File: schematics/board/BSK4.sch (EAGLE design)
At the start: 33 parts

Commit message: Сделаны платы CROSSnew, SPIDERnew, BSK2
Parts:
- removed DS18B20Z: DS18B20Z, CanCubeSat:DS18B20Z
- removed FS8205A#1, FS8205A#2: FS8205A+, CanCubeSat:FS8205A+
- removed L293DD: L293DD, CanCubeSat:L293DD
- removed LAP4: LAP4-BOTTOM, led:LAP4-BOTTOM
- removed LED1, LED2, LED3, LED4, LED5: (no value), led:LEDCHIPLED_0603
- removed R1, R3, R4, R5, R81: 2k, resistor:R-US_R0603
- removed R10, R11, R2, R7: 100R, resistor:R-US_R0603
- removed R19: 1M, resistor:R-US_R0603
- removed R20: 510k, resistor:R-US_R0603
- removed U$6, U$7: EM_HEAT, CanCubeSat:EM_HEAT
- added DS18B20Z1: DS18B20Z, CanCubeSat:DS18B20Z
- added LAP1: LAP4-BOTTOM, led:LAP4-BOTTOM
- added LED6, LED7: (no value), led:LEDCHIPLED_0603
- added R12, R8: 2M, resistor:R-US_R0603
- added R13, R14: 2k, resistor:R-US_R0603
- added R15, R17, R6, R9: 1M, resistor:R-US_R0603
- added R16: 1k5, resistor:R-US_R0603
- added R94, R95: 2k26, resistor:R-US_R0603
- added U$13, U$8: SI2302CDS, CanCubeSat:SI2302CDS
- added U$14: EM_HEAT, CanCubeSat:EM_HEAT
- added U$26: FS8205A+, CanCubeSat:FS8205A+
- added U$5: MOCD217M, CanCubeSat:MOCD217M
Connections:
- removed net N$1: L293DD.OUT1, LED1.C, LED2.A, U$6.5V
- removed net N$10: LED3.C, R3.1
- removed net N$2: L293DD.OUT2, R1.1, R81.1, U$6.GND
- removed net N$27: LAP4.A, LED4.A, R4.2
- removed net N$28: LED5.A, R5.2
- removed net N$3: L293DD.OUT4, LED3.A, U$7.5V
- removed net N$4: FS8205A#2.G1, R2.2
- removed net N$5: LED2.C, R81.2
- removed net N$6: FS8205A#2.G2, R7.2
- removed net N$7: LED1.A, R1.2
- removed net N$8: FS8205A#1.G1, R10.2
- removed net N$9: FS8205A#1.G2, R11.2
- new net 1: R14.2, U$14.GND, U$8.D
- new net 2: R16.2, U$13.D
- new net B4-KHEAT: R15.1, U$8.G
- new net B4-KVCC: R94.2, R95.2, U$5.AN1, U$5.AN2
- new net B4-ROZE: R17.1, U$13.G
- new net N$29: R6.1, R8.2, U$26.G2
- new net N$30: R12.1, R9.1, U$26.G1
- new net N$31: LAP1.A, R13.2
- new net N$32: LED6.C, R14.1
- new net N$33: LED7.C, R16.1
- new net N$34: DS18B20Z1.HEAT, U$26.HEAT
- new net OC1: R9.2, U$5.COL2
- new net OD1: R6.2, U$5.COL1
- net 1W: now also DS18B20Z1.DQ; no longer DS18B20Z.DQ
- net 5V: now also DS18B20Z1.VDD, LED6.A, R13.1, U$14.5V; no longer DS18B20Z.VDD, L293DD.EN1, L293DD.EN2, L293DD.VS, L293DD.VSS, R4.1, R5.1
- net B4_KEM+: no longer L293DD.IN1
- net B4_KEM-: no longer L293DD.IN2
- net B4_KHEAT: no longer L293DD.IN4
- net B4_KVCC: no longer R10.1, R11.1, R19.1, R20.1
- net BUS+: now also LED7.A, R12.2, R8.1; no longer R19.2
- net BUS-: now also LAP1.C, U$26.S2, U$5.EM1; no longer FS8205A#1.S1, LAP4.C, LED4.C, R20.2
- net GND: now also DS18B20Z1.GND, R15.2, R17.2, R94.1, R95.1, U$13.S, U$26.S1, U$5.CAT1, U$5.CAT2, U$5.EM2, U$8.S; no longer DS18B20Z.GND, DS18B20Z.HEAT, FS8205A#1.HEAT, FS8205A#1.S2, FS8205A#2.HEAT, FS8205A#2.S2, L293DD.GND, L293DD.HEAT, R3.2, U$7.GND
- net PL-: no longer FS8205A#2.S1, LED5.C
- net PL_KVCC: no longer R2.1, R7.1
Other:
- note removed: "EM"

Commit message: Плата АB+DC-DC
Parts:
- removed BSK1: (no value), pinheadCS:PINHD-1X14
- removed LAP1: LAP4-BOTTOM, led:LAP4-BOTTOM
- removed PAYLOAD: (no value), pinheadCS:PINHD-1X8
- removed R15, R17: 1M, resistor:R-US_R0603
- removed R16: 1k5, resistor:R-US_R0603
- removed U$18, U$19, U$20, U$21: KCONNECT, CanCubeSat:KCONNECT
- added BKU: (no value), pinheadCS:PINHD-1X11
- added C41: 0,1µ, rcl:C-USC0603
- added CMD: KCONNECTQUAD, CanCubeSat:KCONNECTQUAD
- added R1, R2: 2k26, resistor:R-US_R0603
- added R4, R7: 2k, resistor:R-US_R0603
- added R5: 100R, resistor:R-US_R0603
- added R75: R01, rcl:R-US_R2512
- added R76, R77: 10R, resistor:R-US_R0603
- added U$10, U$11, U$12, U$9: KCONNECT, CanCubeSat:KCONNECT
- added U$15, U$16, U$6, U$7: GRAFITGRAFIT3_1, CanCubeSat:GRAFITGRAFIT3_1
- added U$57: INA219AID, CanCubeSat:INA219AID
- added YELLOW: LAP4-BOTTOM, led:LAP4-BOTTOM
- R12: value 2M -> 100k
- R13: value 2k -> 1k5
- R14: value 2k -> 1M
- R6: value 1M -> 100k
- R8: value 2M -> 1M
- R9: value 1M -> 100R
- R94, R95: value 2k26 -> 200k
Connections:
- net BUS+1 renamed SP+1
- net BUS-1 renamed SP-1
- removed net B4_KEM+: BSK1.11
- removed net B4_KEM-: BSK1.10
- removed net B4_KHEAT: BSK1.12
- removed net B4_KVCC: BSK1.13
- removed net BUS+2: U$18.P$1
- removed net BUS+3: U$20.P$1
- removed net BUS-: LAP1.C, U$2.P$1, U$26.S2, U$5.EM1
- removed net BUS-2: U$19.P$1
- removed net BUS-3: U$21.P$1
- removed net I2CINT: BSK1.5, PAYLOAD.6
- removed net N$32: LED6.C, R14.1
- removed net N$33: LED7.C, R16.1
- removed net N$34: DS18B20Z1.HEAT, U$26.HEAT
- removed net PL-: PAYLOAD.1
- removed net PL_KVCC: BSK1.8
- removed net SCLTM: BSK1.7, PAYLOAD.8
- removed net SDATM: BSK1.6, PAYLOAD.7
- removed net TIME: BSK1.4, PAYLOAD.5
- removed net VDD: BSK1.1, PAYLOAD.2
- new net 3V3: BKU.8, U$57.A1, U$57.VS
- new net B4-CMD: BKU.4, CMD.P$1
- new net N$150: C41.1, R76.2, U$57.IN+
- new net N$151: C41.2, R77.2, U$57.IN-
- new net N$17: R1.1, R94.2, U$5.AN1
- new net N$18: R2.1, R95.2, U$5.AN2
- new net N$26: R5.1, R6.2, U$26.G2
- new net N$28: R4.2, YELLOW.A
- new net SCL-INA: BKU.10, U$57.SCL
- new net SDA-INA: BKU.11, U$57.SDA
- new net SP+: R75.1, R77.1, U$3.P$1
- new net SP+2: U$9.P$1
- new net SP+3: U$11.P$1
- new net SP-: U$2.P$1, U$26.S2, U$5.EM1, YELLOW.C
- new net SP-2: U$10.P$1
- new net SP-3: U$12.P$1
- net 1: now also R7.2; no longer R14.2
- net 1W: now also BKU.5; no longer BSK1.14
- net 2: now also R13.2, U$15.P$1, U$16.P$1, U$6.P$1, U$7.P$1; no longer R16.2
- net 5V: now also BKU.7, R4.1; no longer BSK1.2, PAYLOAD.3, R13.1
- net B4-KHEAT: now also BKU.1, R8.1; no longer R15.1
- net B4-KVCC: now also BKU.2, R1.2, R2.2; no longer R94.2, R95.2, U$5.AN1, U$5.AN2
- net B4-ROZE: now also BKU.3, R14.1; no longer R17.1
- net BUS+: now also BKU.6, R6.1, R75.2, R76.1, U$15.P$2, U$16.P$2, U$6.P$2, U$7.P$2; no longer BSK1.3, PAYLOAD.4, R8.1, U$3.P$1
- net GND: now also BKU.9, DS18B20Z1.HEAT, R14.2, R8.2, U$26.HEAT, U$57.A0, U$57.GND; no longer BSK1.9, R15.2, R17.2
- net N$29: now also LED7.C, R13.1; no longer R6.1, R8.2, U$26.G2
- net N$31: now also LED6.C, R7.1; no longer LAP1.A, R13.2
- net OD1: now also R5.2; no longer R6.2
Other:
- moved on the sheet: LED6, LED7, R12, R13, R14, R6, R8, R9, R94, R95, U$1, U$2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

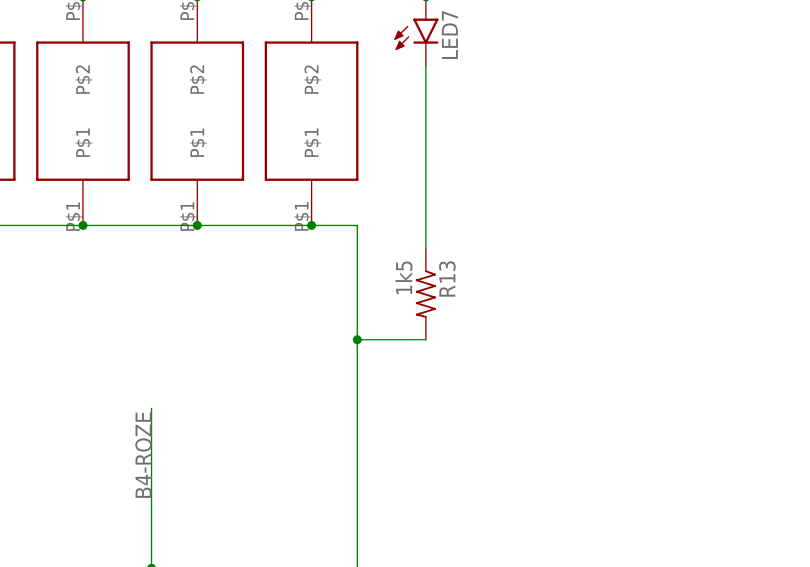
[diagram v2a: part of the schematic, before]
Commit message: Изменен номинал резисторов
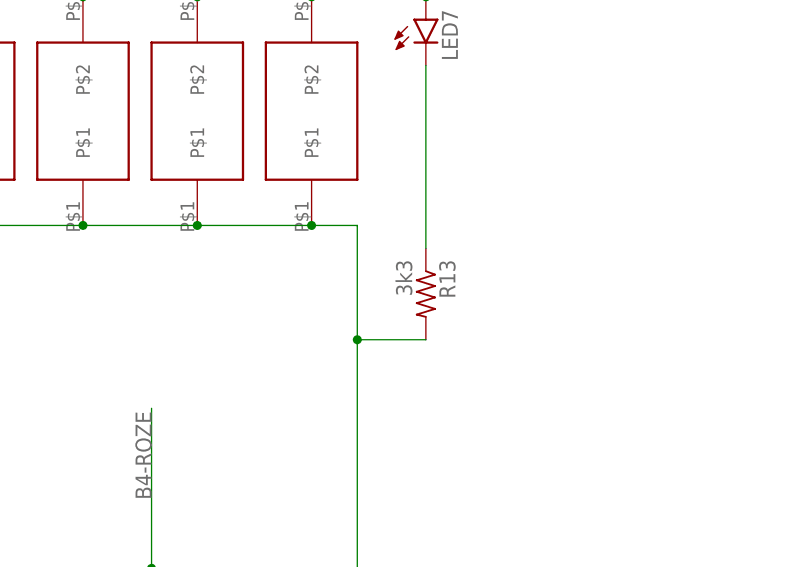
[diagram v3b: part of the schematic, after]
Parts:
- R13: value 1k5 -> 3k3
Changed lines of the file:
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@@
 <part name="R8" library="resistor" library_urn="urn:adsk.eagle:library:348" deviceset="R-US_" device="R0603" package3d_urn="urn:adsk.eagle:package:23555/3" value="1M"/>
 <part name="U$13" library="CanCubeSat" deviceset="SI2302CDS" device=""/>
-<part name="R13" library="resistor" library_urn="urn:adsk.eagle:library:348" deviceset="R-US_" device="R0603" package3d_urn="urn:adsk.eagle:package:23555/3" value="1k5"/>
+<part name="R13" library="resistor" library_urn="urn:adsk.eagle:library:348" deviceset="R-US_" device="R0603" package3d_urn="urn:adsk.eagle:package:23555/3" value="3k3"/>
 <part name="LED7" library="led" library_urn="urn:adsk.eagle:library:259" deviceset="LED" device="CHIPLED_0603" package3d_urn="urn:adsk.eagle:package:15822/2"/>
 <part name="R14" library="resistor" library_urn="urn:adsk.eagle:library:348" deviceset="R-US_" device="R0603" package3d_urn="urn:adsk.eagle:package:23555/3" value="1M"/>

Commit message: Внесены правки в платы БСК
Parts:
- added R3, R32: 100R, resistor:R-US_R0603
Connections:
- new net N$19: R32.1, R8.1, U$8.G
- new net N$20: R14.1, R3.1, U$13.G
- net B4-KHEAT: now also R32.2; no longer R8.1, U$8.G
- net B4-ROZE: now also R3.2; no longer R14.1, U$13.G
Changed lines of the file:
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@@
 <part name="R1" library="resistor" library_urn="urn:adsk.eagle:library:348" deviceset="R-US_" device="R0603" package3d_urn="urn:adsk.eagle:package:23555/3" value="2k26"/>
 <part name="R2" library="resistor" library_urn="urn:adsk.eagle:library:348" deviceset="R-US_" device="R0603" package3d_urn="urn:adsk.eagle:package:23555/3" value="2k26"/>
+<part name="R32" library="resistor" deviceset="R-US_" device="R0603" package3d_urn="urn:adsk.eagle:package:23555/3" value="100R"/>
+<part name="R3" library="resistor" deviceset="R-US_" device="R0603" package3d_urn="urn:adsk.eagle:package:23555/3" value="100R"/>
 </parts>
 <sheets>
@@
 <attribute name="VALUE" x="-126.238" y="285.75" size="1.778" layer="96" rot="R90"/>
 </instance>
+<instance part="R32" gate="G$1" x="-177.8" y="96.52" smashed="yes" rot="R90">
+<attribute name="NAME" x="-179.2986" y="92.71" size="1.778" layer="95" rot="R90"/>
+<attribute name="VALUE" x="-174.498" y="92.71" size="1.778" layer="96" rot="R90"/>
+</instance>
+<instance part="R3" gate="G$1" x="-81.28" y="96.52" smashed="yes" rot="R90">
+<attribute name="NAME" x="-82.7786" y="92.71" size="1.778" layer="95" rot="R90"/>
+<attribute name="VALUE" x="-77.978" y="92.71" size="1.778" layer="96" rot="R90"/>
+</instance>
 </instances>
 <busses>
@@
 <net name="B4-ROZE" class="0">
 <segment>
-<pinref part="R14" gate="G$1" pin="1"/>
-<wire x1="-96.52" y1="88.9" x2="-81.28" y2="88.9" width="0.1524" layer="91"/>
-<pinref part="U$13" gate="G$1" pin="G"/>
-<wire x1="-81.28" y1="88.9" x2="-81.28" y2="86.36" width="0.1524" layer="91"/>
-<wire x1="-81.28" y1="88.9" x2="-81.28" y2="106.68" width="0.1524" layer="91"/>
-<junction x="-81.28" y="88.9"/>
-<label x="-81.28" y="96.52" size="1.778" layer="95" rot="R90"/>
-</segment>
-<segment>
 <wire x1="149.86" y1="177.8" x2="149.86" y2="198.12" width="0.1524" layer="91"/>
 <label x="149.86" y="185.42" size="1.778" layer="95" rot="R90"/>
 <pinref part="BKU" gate="A" pin="3"/>
+</segment>
+<segment>
+<pinref part="R3" gate="G$1" pin="2"/>
+<wire x1="-81.28" y1="114.3" x2="-81.28" y2="101.6" width="0.1524" layer="91"/>
+<label x="-81.28" y="104.14" size="1.778" layer="95" rot="R90"/>
 </segment>
 </net>
@@
 <net name="B4-KHEAT" class="0">
 <segment>
-<pinref part="R8" gate="G$1" pin="1"/>
-<wire x1="-193.04" y1="88.9" x2="-177.8" y2="88.9" width="0.1524" layer="91"/>
-<pinref part="U$8" gate="G$1" pin="G"/>
-<wire x1="-177.8" y1="88.9" x2="-177.8" y2="86.36" width="0.1524" layer="91"/>
-<wire x1="-177.8" y1="88.9" x2="-177.8" y2="106.68" width="0.1524" layer="91"/>
-<junction x="-177.8" y="88.9"/>
-<label x="-177.8" y="96.52" size="1.778" layer="95" rot="R90"/>
-</segment>
-<segment>
 <wire x1="144.78" y1="177.8" x2="144.78" y2="198.12" width="0.1524" layer="91"/>
 <label x="144.78" y="185.42" size="1.778" layer="95" rot="R90"/>
 <pinref part="BKU" gate="A" pin="1"/>
+</segment>
+<segment>
+<pinref part="R32" gate="G$1" pin="2"/>
+<wire x1="-177.8" y1="101.6" x2="-177.8" y2="114.3" width="0.1524" layer="91"/>
+<label x="-177.8" y="104.14" size="1.778" layer="95" rot="R90"/>
 </segment>
 </net>
@@
 </segment>
 </net>
+<net name="N$19" class="0">
+<segment>
+<pinref part="R32" gate="G$1" pin="1"/>
+<pinref part="U$8" gate="G$1" pin="G"/>
+<wire x1="-177.8" y1="91.44" x2="-177.8" y2="88.9" width="0.1524" layer="91"/>
+<pinref part="R8" gate="G$1" pin="1"/>
+<wire x1="-177.8" y1="88.9" x2="-177.8" y2="86.36" width="0.1524" layer="91"/>
+<wire x1="-193.04" y1="88.9" x2="-177.8" y2="88.9" width="0.1524" layer="91"/>
+<junction x="-177.8" y="88.9"/>
+</segment>
+</net>
+<net name="N$20" class="0">
+<segment>
+<pinref part="R3" gate="G$1" pin="1"/>
+<pinref part="U$13" gate="G$1" pin="G"/>
+<wire x1="-81.28" y1="91.44" x2="-81.28" y2="88.9" width="0.1524" layer="91"/>
+<pinref part="R14" gate="G$1" pin="1"/>
+<wire x1="-81.28" y1="88.9" x2="-81.28" y2="86.36" width="0.1524" layer="91"/>
+<wire x1="-96.52" y1="88.9" x2="-81.28" y2="88.9" width="0.1524" layer="91"/>
+<junction x="-81.28" y="88.9"/>
+</segment>
+</net>

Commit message: Две линии i2c на платах БСК заменены на одну
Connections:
- net SCL-INA renamed SCL-TM
- net SDA-INA renamed SDA-TM
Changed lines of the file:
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@@
 </segment>
 </net>
-<net name="SCL-INA" class="0">
+<net name="SCL-TM" class="0">
 <segment>
 <wire x1="-273.05" y1="220.98" x2="-273.05" y2="231.14" width="0.1524" layer="91"/>
@@
 </segment>
 </net>
-<net name="SDA-INA" class="0">
+<net name="SDA-TM" class="0">
 <segment>
 <wire x1="-270.51" y1="220.98" x2="-270.51" y2="228.6" width="0.1524" layer="91"/>
